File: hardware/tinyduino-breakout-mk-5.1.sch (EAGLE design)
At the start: 12 parts, among them J1 DF12-32-DP-NOTREALLYREV

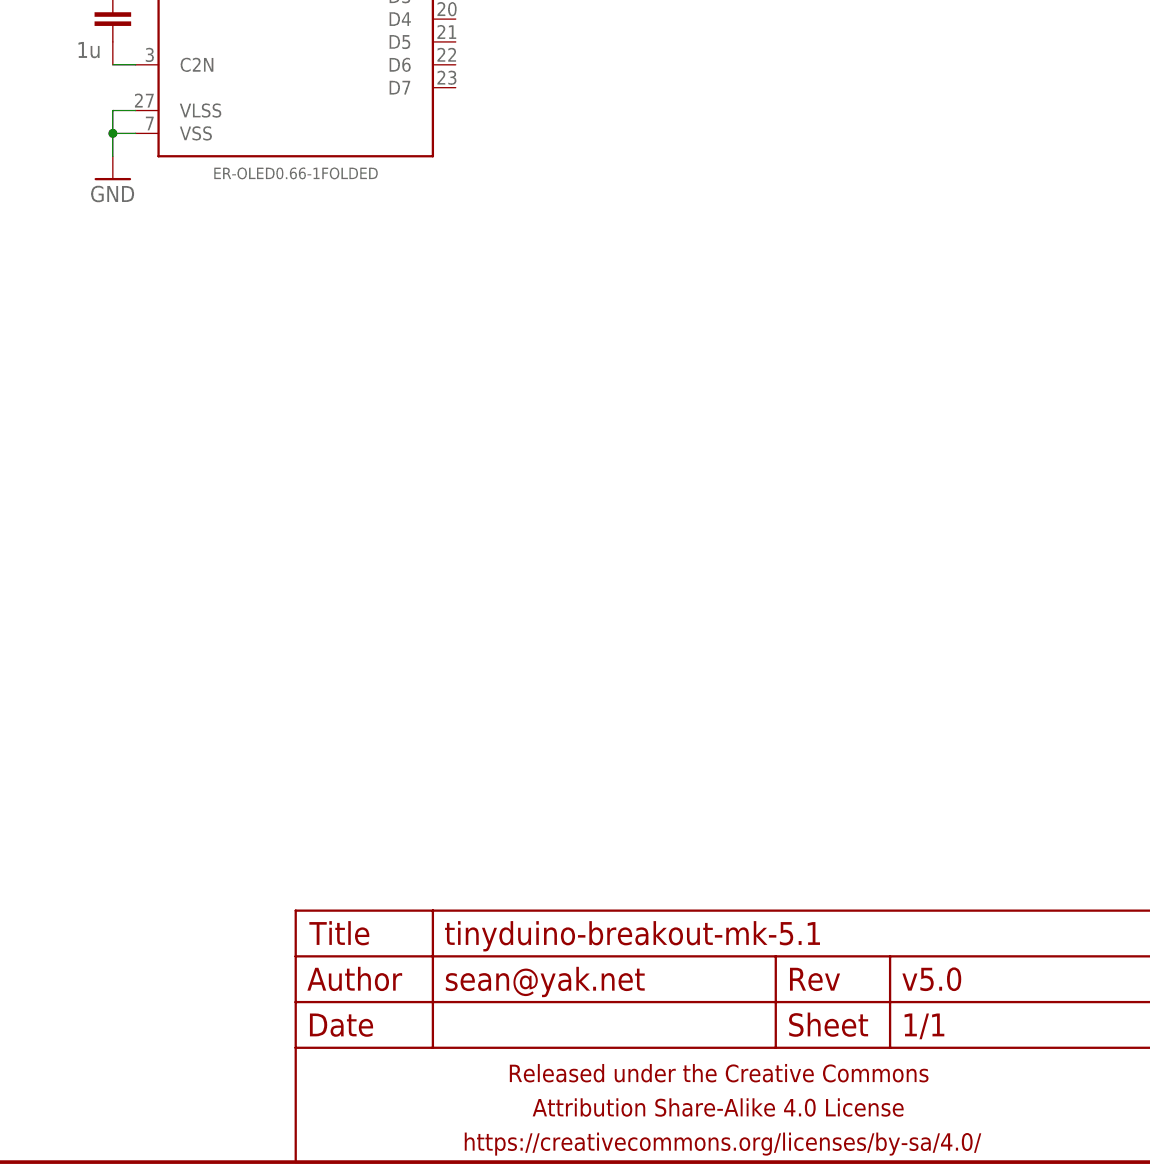
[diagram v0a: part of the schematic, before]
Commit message: breakouts for the tinyduino version
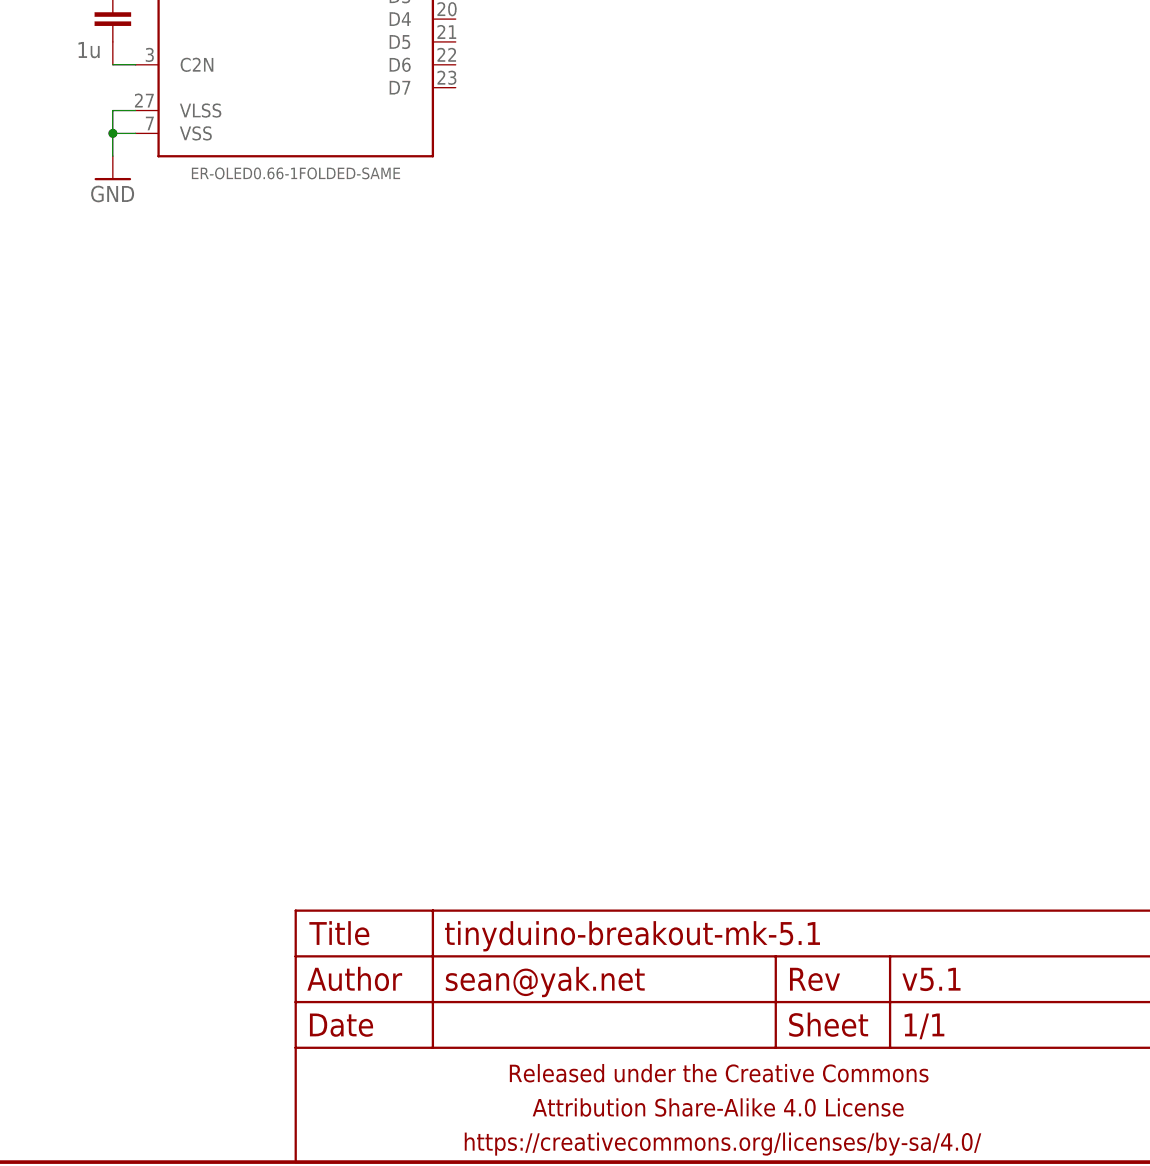
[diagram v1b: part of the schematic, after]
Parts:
- DISP1: value ER-OLED0.66-1FOLDED -> ER-OLED0.66-1FOLDED-SAME; device a_parts:ER-OLED0.66-1FOLDED -> a_parts:ER-OLED0.66-1FOLDED-SAME
- FRAME1: VERSION v5.0 -> v5.1
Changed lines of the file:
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@@
 <grid distance="0.1" unitdist="inch" unit="mil" style="lines" multiple="1" display="yes" altdistance="0.01" altunitdist="inch" altunit="inch"/>
 <layers>
-<layer number="1" name="Top" color="4" fill="1" visible="no" active="no"/>
-<layer number="16" name="Bottom" color="1" fill="1" visible="no" active="no"/>
-<layer number="17" name="Pads" color="2" fill="1" visible="no" active="no"/>
-<layer number="18" name="Vias" color="2" fill="1" visible="no" active="no"/>
-<layer number="19" name="Unrouted" color="6" fill="1" visible="no" active="no"/>
-<layer number="20" name="Dimension" color="15" fill="1" visible="no" active="no"/>
-<layer number="21" name="tPlace" color="7" fill="1" visible="no" active="no"/>
-<layer number="22" name="bPlace" color="7" fill="1" visible="no" active="no"/>
-<layer number="23" name="tOrigins" color="15" fill="1" visible="no" active="no"/>
-<layer number="24" name="bOrigins" color="15" fill="1" visible="no" active="no"/>
-<layer number="25" name="tNames" color="7" fill="1" visible="no" active="no"/>
-<layer number="26" name="bNames" color="7" fill="1" visible="no" active="no"/>
-<layer number="27" name="tValues" color="7" fill="1" visible="no" active="no"/>
-<layer number="28" name="bValues" color="7" fill="1" visible="no" active="no"/>
+<layer number="1" name="Top" color="4" fill="1" visible="yes" active="no"/>
+<layer number="16" name="Bottom" color="1" fill="1" visible="yes" active="no"/>
+<layer number="17" name="Pads" color="2" fill="1" visible="yes" active="no"/>
+<layer number="18" name="Vias" color="2" fill="1" visible="yes" active="no"/>
+<layer number="19" name="Unrouted" color="6" fill="1" visible="yes" active="no"/>
+<layer number="20" name="Dimension" color="15" fill="1" visible="yes" active="no"/>
+<layer number="21" name="tPlace" color="7" fill="1" visible="yes" active="no"/>
+<layer number="22" name="bPlace" color="7" fill="1" visible="yes" active="no"/>
+<layer number="23" name="tOrigins" color="15" fill="1" visible="yes" active="no"/>
+<layer number="24" name="bOrigins" color="15" fill="1" visible="yes" active="no"/>
+<layer number="25" name="tNames" color="7" fill="1" visible="yes" active="no"/>
+<layer number="26" name="bNames" color="7" fill="1" visible="yes" active="no"/>
+<layer number="27" name="tValues" color="7" fill="1" visible="yes" active="no"/>
+<layer number="28" name="bValues" color="7" fill="1" visible="yes" active="no"/>
 <layer number="29" name="tStop" color="7" fill="3" visible="no" active="no"/>
 <layer number="30" name="bStop" color="7" fill="6" visible="no" active="no"/>
@@
 <layer number="35" name="tGlue" color="7" fill="4" visible="no" active="no"/>
 <layer number="36" name="bGlue" color="7" fill="5" visible="no" active="no"/>
-<layer number="37" name="tTest" color="7" fill="1" visible="no" active="no"/>
-<layer number="38" name="bTest" color="7" fill="1" visible="no" active="no"/>
+<layer number="37" name="tTest" color="7" fill="1" visible="yes" active="no"/>
+<layer number="38" name="bTest" color="7" fill="1" visible="yes" active="no"/>
 <layer number="39" name="tKeepout" color="4" fill="11" visible="no" active="no"/>
 <layer number="40" name="bKeepout" color="1" fill="11" visible="no" active="no"/>
@@
 <layer number="44" name="Drills" color="7" fill="1" visible="no" active="no"/>
 <layer number="45" name="Holes" color="7" fill="1" visible="no" active="no"/>
-<layer number="46" name="Milling" color="3" fill="1" visible="no" active="no"/>
-<layer number="47" name="Measures" color="7" fill="1" visible="no" active="no"/>
-<layer number="48" name="Document" color="7" fill="1" visible="no" active="no"/>
-<layer number="49" name="Reference" color="7" fill="1" visible="no" active="no"/>
-<layer number="50" name="dxf" color="7" fill="1" visible="no" active="no"/>
-<layer number="51" name="tDocu" color="7" fill="1" visible="no" active="no"/>
-<layer number="52" name="bDocu" color="7" fill="1" visible="no" active="no"/>
-<layer number="53" name="tGND_GNDA" color="7" fill="9" visible="no" active="no"/>
-<layer number="54" name="bGND_GNDA" color="1" fill="9" visible="no" active="no"/>
-<layer number="56" name="wert" color="7" fill="1" visible="no" active="no"/>
-<layer number="57" name="tCAD" color="7" fill="1" visible="no" active="no"/>
-<layer number="59" name="tCarbon" color="7" fill="1" visible="no" active="no"/>
-<layer number="60" name="bCarbon" color="7" fill="1" visible="no" active="no"/>
+<layer number="46" name="Milling" color="3" fill="1" visible="yes" active="no"/>
+<layer number="47" name="Measures" color="7" fill="1" visible="yes" active="no"/>
+<layer number="48" name="Document" color="7" fill="1" visible="yes" active="no"/>
+<layer number="49" name="Reference" color="7" fill="1" visible="yes" active="no"/>
+<layer number="50" name="dxf" color="7" fill="1" visible="yes" active="no"/>
+<layer number="51" name="tDocu" color="7" fill="1" visible="yes" active="no"/>
+<layer number="52" name="bDocu" color="7" fill="1" visible="yes" active="no"/>
+<layer number="53" name="tGND_GNDA" color="7" fill="9" visible="yes" active="no"/>
+<layer number="54" name="bGND_GNDA" color="1" fill="9" visible="yes" active="no"/>
+<layer number="56" name="wert" color="7" fill="1" visible="yes" active="no"/>
+<layer number="57" name="tCAD" color="7" fill="1" visible="yes" active="no"/>
+<layer number="59" name="tCarbon" color="7" fill="1" visible="yes" active="no"/>
+<layer number="60" name="bCarbon" color="7" fill="1" visible="yes" active="no"/>
 <layer number="90" name="Modules" color="5" fill="1" visible="yes" active="yes"/>
 <layer number="91" name="Nets" color="2" fill="1" visible="yes" active="yes"/>
@@
 <part name="FRAME1" library="A_butts" deviceset="FRAME-LETTER" device="NO_PACKAGE">
 <attribute name="DESIGNER" value="sean@yak.net"/>
-<attribute name="VERSION" value="v5.0"/>
+<attribute name="VERSION" value="v5.1"/>
 </part>
 <part name="SUPPLY3" library="SparkFun-Aesthetics" deviceset="VCC" device=""/>
 <part name="GND3" library="SparkFun-Aesthetics" deviceset="GND" device=""/>
 <part name="J1" library="a_parts" deviceset="DF12-32-DP-NOTREALLY" device="REV" value="DF12-32-DP-NOTREALLYREV"/>
-<part name="DISP1" library="a_parts" deviceset="ER-OLED0.66-1" device="FOLDED"/>
+<part name="DISP1" library="a_parts" deviceset="ER-OLED0.66-1" device="FOLDED-SAME" value="ER-OLED0.66-1FOLDED-SAME"/>
 <part name="C1" library="a_parts" deviceset="CAPACITOR-CERAMIC" device="C0603" value="1u"/>
 <part name="C2" library="a_parts" deviceset="CAPACITOR-CERAMIC" device="C0603" value="2u2"/>
